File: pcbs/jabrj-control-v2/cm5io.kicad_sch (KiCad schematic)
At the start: 22 parts, among them J801 48406-0003, J802 ARJM11D7-502-AB-EW2, J803 TYPE-C-31-M-12, U801 PESD4USB3BTTS-QX, U802 PESD4USB3BTTS-QX, U803 PESD4USB3BTTS-QX, U804 PESD4USB3BTTS-QX, U805 PESD4USB3BTTS-QX, U806 AP22653FDZ-7, U807 PESD4USB3BTTS-QX

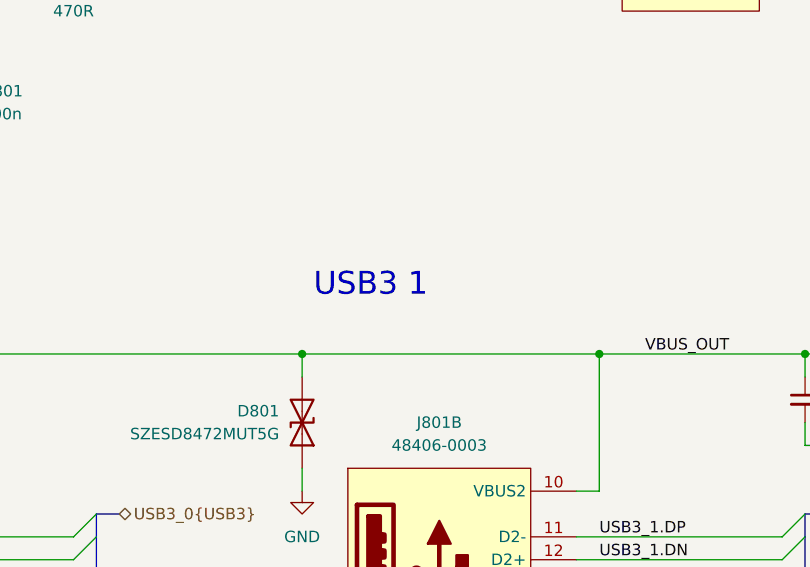
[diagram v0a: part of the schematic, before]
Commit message: Fixed 5V buck inductor value
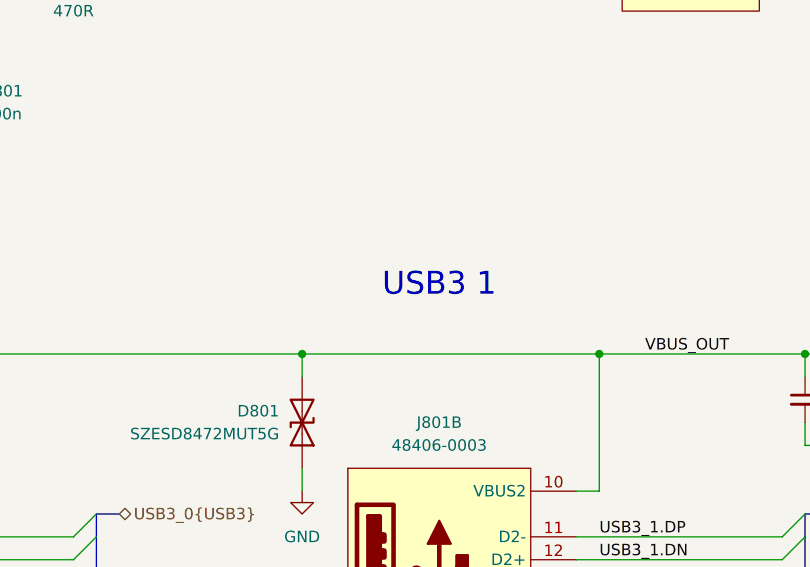
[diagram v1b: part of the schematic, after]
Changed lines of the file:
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@@
 	(text "USB3 1"
 		(exclude_from_sim no)
-		(at 111.76 111.76 0)
+		(at 119.38 111.76 0)
 		(effects
 			(font
@@
 		)
 		(instances
-			(project "jabr-control-v2"
+			(project "jabrj-control-v2"
 				(path "/f91ec272-d09a-4038-bbbb-962739a92c51/adc0b005-3094-4656-96e7-4ee9fb2ab719"
 					(reference "C804")
@@
 		)
 		(instances
-			(project "jabr-control-v2"
+			(project "jabrj-control-v2"
 				(path "/f91ec272-d09a-4038-bbbb-962739a92c51/adc0b005-3094-4656-96e7-4ee9fb2ab719"
 					(reference "#PWR0801")
@@
 		)
 		(instances
-			(project "jabr-control-v2"
+			(project "jabrj-control-v2"
 				(path "/f91ec272-d09a-4038-bbbb-962739a92c51/adc0b005-3094-4656-96e7-4ee9fb2ab719"
 					(reference "J803")
@@
 		)
 		(instances
-			(project "jabr-control-v2"
+			(project "jabrj-control-v2"
 				(path "/f91ec272-d09a-4038-bbbb-962739a92c51/adc0b005-3094-4656-96e7-4ee9fb2ab719"
 					(reference "#PWR0810")
@@
 		)
 		(instances
-			(project "jabr-control-v2"
+			(project "jabrj-control-v2"
 				(path "/f91ec272-d09a-4038-bbbb-962739a92c51/adc0b005-3094-4656-96e7-4ee9fb2ab719"
 					(reference "#PWR0809")
@@
 		)
 		(instances
-			(project "jabr-control-v2"
+			(project "jabrj-control-v2"
 				(path "/f91ec272-d09a-4038-bbbb-962739a92c51/adc0b005-3094-4656-96e7-4ee9fb2ab719"
 					(reference "C807")
@@
 		)
 		(instances
-			(project "jabr-control-v2"
+			(project "jabrj-control-v2"
 				(path "/f91ec272-d09a-4038-bbbb-962739a92c51/adc0b005-3094-4656-96e7-4ee9fb2ab719"
 					(reference "#PWR0817")
@@
 		)
 		(instances
-			(project "jabr-control-v2"
+			(project "jabrj-control-v2"
 				(path "/f91ec272-d09a-4038-bbbb-962739a92c51/adc0b005-3094-4656-96e7-4ee9fb2ab719"
 					(reference "C806")
@@
 		)
 		(instances
-			(project "jabr-control-v2"
+			(project "jabrj-control-v2"
 				(path "/f91ec272-d09a-4038-bbbb-962739a92c51/adc0b005-3094-4656-96e7-4ee9fb2ab719"
 					(reference "U801")
@@
 		)
 		(instances
-			(project "jabr-control-v2"
+			(project "jabrj-control-v2"
 				(path "/f91ec272-d09a-4038-bbbb-962739a92c51/adc0b005-3094-4656-96e7-4ee9fb2ab719"
 					(reference "C801")
@@
 		)
 		(instances
-			(project "jabr-control-v2"
+			(project "jabrj-control-v2"
 				(path "/f91ec272-d09a-4038-bbbb-962739a92c51/adc0b005-3094-4656-96e7-4ee9fb2ab719"
 					(reference "U802")
@@
 		)
 		(instances
-			(project "jabr-control-v2"
+			(project "jabrj-control-v2"
 				(path "/f91ec272-d09a-4038-bbbb-962739a92c51/adc0b005-3094-4656-96e7-4ee9fb2ab719"
 					(reference "#PWR0815")
@@
 		)
 		(instances
-			(project "jabr-control-v2"
+			(project "jabrj-control-v2"
 				(path "/f91ec272-d09a-4038-bbbb-962739a92c51/adc0b005-3094-4656-96e7-4ee9fb2ab719"
 					(reference "D801")
@@
 		)
 		(instances
-			(project "jabr-control-v2"
+			(project "jabrj-control-v2"
 				(path "/f91ec272-d09a-4038-bbbb-962739a92c51/adc0b005-3094-4656-96e7-4ee9fb2ab719"
 					(reference "C805")
@@
 		)
 		(instances
-			(project "jabr-control-v2"
+			(project "jabrj-control-v2"
 				(path "/f91ec272-d09a-4038-bbbb-962739a92c51/adc0b005-3094-4656-96e7-4ee9fb2ab719"
 					(reference "#PWR0808")
@@
 		)
 		(instances
-			(project "jabr-control-v2"
+			(project "jabrj-control-v2"
 				(path "/f91ec272-d09a-4038-bbbb-962739a92c51/adc0b005-3094-4656-96e7-4ee9fb2ab719"
 					(reference "#PWR0812")
@@
 		)
 		(instances
-			(project "jabr-control-v2"
+			(project "jabrj-control-v2"
 				(path "/f91ec272-d09a-4038-bbbb-962739a92c51/adc0b005-3094-4656-96e7-4ee9fb2ab719"
 					(reference "C803")
@@
 		)
 		(instances
-			(project "jabr-control-v2"
+			(project "jabrj-control-v2"
 				(path "/f91ec272-d09a-4038-bbbb-962739a92c51/adc0b005-3094-4656-96e7-4ee9fb2ab719"
 					(reference "#PWR0807")
@@
 		)
 		(instances
-			(project "jabr-control-v2"
+			(project "jabrj-control-v2"
 				(path "/f91ec272-d09a-4038-bbbb-962739a92c51/adc0b005-3094-4656-96e7-4ee9fb2ab719"
 					(reference "#PWR0802")
@@
 		)
 		(instances
-			(project "jabr-control-v2"
+			(project "jabrj-control-v2"
 				(path "/f91ec272-d09a-4038-bbbb-962739a92c51/adc0b005-3094-4656-96e7-4ee9fb2ab719"
 					(reference "U806")
@@
 		)
 		(instances
-			(project "jabr-control-v2"
+			(project "jabrj-control-v2"
 				(path "/f91ec272-d09a-4038-bbbb-962739a92c51/adc0b005-3094-4656-96e7-4ee9fb2ab719"
 					(reference "D802")
@@
 		)
 		(instances
-			(project "jabr-control-v2"
+			(project "jabrj-control-v2"
 				(path "/f91ec272-d09a-4038-bbbb-962739a92c51/adc0b005-3094-4656-96e7-4ee9fb2ab719"
 					(reference "C802")
@@
 		)
 		(instances
-			(project "jabr-control-v2"
+			(project "jabrj-control-v2"
 				(path "/f91ec272-d09a-4038-bbbb-962739a92c51/adc0b005-3094-4656-96e7-4ee9fb2ab719"
 					(reference "#PWR0806")
@@
 		)
 		(instances
-			(project "jabr-control-v2"
+			(project "jabrj-control-v2"
 				(path "/f91ec272-d09a-4038-bbbb-962739a92c51/adc0b005-3094-4656-96e7-4ee9fb2ab719"
 					(reference "#PWR0805")
@@
 		)
 		(instances
-			(project "jabr-control-v2"
+			(project "jabrj-control-v2"
 				(path "/f91ec272-d09a-4038-bbbb-962739a92c51/adc0b005-3094-4656-96e7-4ee9fb2ab719"
 					(reference "U805")
@@
 		)
 		(instances
-			(project "jabr-control-v2"
+			(project "jabrj-control-v2"
 				(path "/f91ec272-d09a-4038-bbbb-962739a92c51/adc0b005-3094-4656-96e7-4ee9fb2ab719"
 					(reference "#PWR0804")
@@
 		)
 		(instances
-			(project "jabr-control-v2"
+			(project "jabrj-control-v2"
 				(path "/f91ec272-d09a-4038-bbbb-962739a92c51/adc0b005-3094-4656-96e7-4ee9fb2ab719"
 					(reference "U804")
@@
 		)
 		(instances
-			(project "jabr-control-v2"
+			(project "jabrj-control-v2"
 				(path "/f91ec272-d09a-4038-bbbb-962739a92c51/adc0b005-3094-4656-96e7-4ee9fb2ab719"
 					(reference "#PWR0813")
@@
 		)
 		(instances
-			(project "jabr-control-v2"
+			(project "jabrj-control-v2"
 				(path "/f91ec272-d09a-4038-bbbb-962739a92c51/adc0b005-3094-4656-96e7-4ee9fb2ab719"
 					(reference "#PWR0814")
@@
 		)
 		(instances
-			(project "jabr-control-v2"
+			(project "jabrj-control-v2"
 				(path "/f91ec272-d09a-4038-bbbb-962739a92c51/adc0b005-3094-4656-96e7-4ee9fb2ab719"
 					(reference "J802")
@@
 		)
 		(instances
-			(project "jabr-control-v2"
+			(project "jabrj-control-v2"
 				(path "/f91ec272-d09a-4038-bbbb-962739a92c51/adc0b005-3094-4656-96e7-4ee9fb2ab719"
 					(reference "#PWR0816")
@@
 		)
 		(instances
-			(project "jabr-control-v2"
+			(project "jabrj-control-v2"
 				(path "/f91ec272-d09a-4038-bbbb-962739a92c51/adc0b005-3094-4656-96e7-4ee9fb2ab719"
 					(reference "#PWR0803")
@@
 		)
 		(instances
-			(project "jabr-control-v2"
+			(project "jabrj-control-v2"
 				(path "/f91ec272-d09a-4038-bbbb-962739a92c51/adc0b005-3094-4656-96e7-4ee9fb2ab719"
 					(reference "R803")
@@
 		)
 		(instances
-			(project "jabr-control-v2"
+			(project "jabrj-control-v2"
 				(path "/f91ec272-d09a-4038-bbbb-962739a92c51/adc0b005-3094-4656-96e7-4ee9fb2ab719"
 					(reference "#PWR0818")
@@
 		)
 		(instances
-			(project "jabr-control-v2"
+			(project "jabrj-control-v2"
 				(path "/f91ec272-d09a-4038-bbbb-962739a92c51/adc0b005-3094-4656-96e7-4ee9fb2ab719"
 					(reference "R802")
@@
 		)
 		(instances
-			(project "jabr-control-v2"
+			(project "jabrj-control-v2"
 				(path "/f91ec272-d09a-4038-bbbb-962739a92c51/adc0b005-3094-4656-96e7-4ee9fb2ab719"
 					(reference "U803")
@@
 		)
 		(instances
-			(project "jabr-control-v2"
+			(project "jabrj-control-v2"
 				(path "/f91ec272-d09a-4038-bbbb-962739a92c51/adc0b005-3094-4656-96e7-4ee9fb2ab719"
 					(reference "J801")
@@
 		)
 		(instances
-			(project "jabr-control-v2"
+			(project "jabrj-control-v2"
 				(path "/f91ec272-d09a-4038-bbbb-962739a92c51/adc0b005-3094-4656-96e7-4ee9fb2ab719"
 					(reference "#PWR0811")
@@
 		)
 		(instances
-			(project "jabr-control-v2"
+			(project "jabrj-control-v2"
 				(path "/f91ec272-d09a-4038-bbbb-962739a92c51/adc0b005-3094-4656-96e7-4ee9fb2ab719"
 					(reference "J801")
@@
 		)
 		(instances
-			(project "jabr-control-v2"
+			(project "jabrj-control-v2"
 				(path "/f91ec272-d09a-4038-bbbb-962739a92c51/adc0b005-3094-4656-96e7-4ee9fb2ab719"
 					(reference "U807")
@@
 		)
 		(instances
-			(project "jabr-control-v2"
+			(project "jabrj-control-v2"
 				(path "/f91ec272-d09a-4038-bbbb-962739a92c51/adc0b005-3094-4656-96e7-4ee9fb2ab719"
 					(reference "R801")

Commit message: Layout started
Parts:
- added J804, J805: FH12-20S-0.5SH, project_footprints:Hirose_FH12-20S-0.5SH_1x20-1MP_P0.50mm_Horizontal, symbol CONN-FPC:FH12-20S-0.5SH
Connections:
- net GND: now also J804.11, J804.14, J804.17, J804.2, J804.20, J804.5, J804.8, J804.MP1, J804.MP2, J805.MP1, J805.MP2
- net USB3_0.DN: now also U805.2 (CH2), U805.9 (NC), J804.4; no longer U802.2 (CH2), U802.9 (NC)
- net USB3_0.DP: now also U805.1 (CH1), U805.10 (NC), J804.3; no longer U802.1 (CH1), U802.10 (NC)
- net USB3_0.RX_N: now also J804.7
- net USB3_0.RX_P: now also J804.6
- net USB3_0.TX_N: now also J804.10
- net USB3_0.TX_P: now also J804.9
- net USB3_1.DN: now also J804.13
- net USB3_1.DP: now also J804.12
- net USB3_1.RX_N: now also U802.2 (CH2), U802.9 (NC), J804.16; no longer U805.2 (CH2), U805.9 (NC)
- net USB3_1.RX_P: now also U802.1 (CH1), U802.10 (NC), J804.15; no longer U805.1 (CH1), U805.10 (NC)
- net USB3_1.TX_N: now also J804.19
- net USB3_1.TX_P: now also J804.18
- net VBUS_EN: now also J804.1

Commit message: Layout almost done
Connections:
- net USB.CC1: now also U807.5 (CH4), U807.6 (NC); no longer U807.2 (CH2), U807.9 (NC)
- net USB.DP: now also U807.2 (CH2), U807.9 (NC); no longer U807.5 (CH4), U807.6 (NC)
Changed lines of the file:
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@@
-	)
-	(junction
-		(at 226.06 50.8)
-		(diameter 0)
-		(color 0 0 0 0)
 	)
 	(junction
@@
 	)
 	(junction
-		(at 231.14 60.96)
-		(diameter 0)
-		(color 0 0 0 0)
-	)
-	(junction
 		(at 66.04 86.36)
 		(diameter 0)
@@
 	)
 	(junction
+		(at 226.06 60.96)
+		(diameter 0)
+		(color 0 0 0 0)
+	)
+	(junction
 		(at 223.52 40.64)
 		(diameter 0)
@@
 	(junction
 		(at 63.5 185.42)
+		(diameter 0)
+		(color 0 0 0 0)
+	)
+	(junction
+		(at 231.14 50.8)
 		(diameter 0)
 		(color 0 0 0 0)
@@
 	(wire
 		(pts
-			(xy 231.14 60.96) (xy 231.14 81.28)
-		)
-		(stroke
-			(width 0)
-			(type default)
-		)
-	)
-	(wire
-		(pts
 			(xy 233.68 78.74) (xy 236.22 78.74)
 		)
@@
 	(wire
 		(pts
-			(xy 223.52 50.8) (xy 226.06 50.8)
+			(xy 223.52 50.8) (xy 231.14 50.8)
 		)
 		(stroke
@@
 	(wire
 		(pts
+			(xy 231.14 50.8) (xy 231.14 81.28)
+		)
+		(stroke
+			(width 0)
+			(type default)
+		)
+	)
+	(wire
+		(pts
 			(xy 208.28 129.54) (xy 208.28 132.08)
 		)
@@
 	(wire
 		(pts
+			(xy 226.06 60.96) (xy 226.06 86.36)
+		)
+		(stroke
+			(width 0)
+			(type default)
+		)
+	)
+	(wire
+		(pts
 			(xy 55.88 142.24) (xy 78.74 142.24)
 		)
@@
 	(wire
 		(pts
-			(xy 231.14 60.96) (xy 248.92 60.96)
-		)
-		(stroke
-			(width 0)
-			(type default)
-		)
-	)
-	(wire
-		(pts
 			(xy 162.56 76.2) (xy 160.02 76.2)
 		)
@@
 		)
 	)
-	(wire
-		(pts
-			(xy 226.06 50.8) (xy 248.92 50.8)
-		)
-		(stroke
-			(width 0)
-			(type default)
-		)
-	)
 	(bus
 		(pts
@@
 	(wire
 		(pts
+			(xy 226.06 60.96) (xy 248.92 60.96)
+		)
+		(stroke
+			(width 0)
+			(type default)
+		)
+	)
+	(wire
+		(pts
 			(xy 58.42 119.38) (xy 104.14 119.38)
 		)
@@
 	(wire
 		(pts
-			(xy 220.98 60.96) (xy 231.14 60.96)
+			(xy 220.98 60.96) (xy 226.06 60.96)
 		)
 		(stroke
@@
 	(wire
 		(pts
+			(xy 231.14 50.8) (xy 248.92 50.8)
+		)
+		(stroke
+			(width 0)
+			(type default)
+		)
+	)
+	(wire
+		(pts
 			(xy 220.98 43.18) (xy 223.52 43.18)
 		)
 		(stroke
-			(width 0)
-			(type default)
-		)
-	)
-	(wire
-		(pts
-			(xy 226.06 50.8) (xy 226.06 86.36)
-		)
-		(stroke

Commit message: 603 Unrouted
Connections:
- net USB3_0.DN: now also J801.2 (D1-), J804.6, U801.4 (CH3), U801.7 (NC); no longer J801.3 (D1+), J804.4, U805.2 (CH2), U805.9 (NC)
- net USB3_0.DP: now also J801.3 (D1+), J804.7, U801.5 (CH4), U801.6 (NC); no longer J801.2 (D1-), J804.3, U805.1 (CH1), U805.10 (NC)
- net USB3_0.RX_N: now also J801.5 (SSRX1-), J804.10, U805.2 (CH2), U805.9 (NC); no longer J801.6 (SSRX1+), J804.7, U801.2 (CH2), U801.9 (NC)
- net USB3_0.RX_P: now also J801.6 (SSRX1+), J804.9, U805.1 (CH1), U805.10 (NC); no longer J801.5 (SSRX1-), J804.6, U801.1 (CH1), U801.10 (NC)
- net USB3_0.TX_N: now also J801.8 (SSTX1-), J804.4, U801.2 (CH2), U801.9 (NC); no longer J801.9 (SSTX1+), J804.10, U801.5 (CH4), U801.6 (NC)
- net USB3_0.TX_P: now also J801.9 (SSTX1+), J804.3, U801.1 (CH1), U801.10 (NC); no longer J801.8 (SSTX1-), J804.9, U801.4 (CH3), U801.7 (NC)
- net USB3_1.DN: now also J801.11 (D2-), J804.16, U802.2 (CH2), U802.9 (NC); no longer J801.12 (D2+), J804.13, U802.5 (CH4), U802.6 (NC)
- net USB3_1.DP: now also J801.12 (D2+), J804.15, U802.1 (CH1), U802.10 (NC); no longer J801.11 (D2-), J804.12, U802.4 (CH3), U802.7 (NC)
- net USB3_1.RX_N: now also J801.14 (SSRX2-), J804.12, U805.4 (CH3), U805.7 (NC); no longer J801.15 (SSRX2+), J804.16, U802.2 (CH2), U802.9 (NC)
- net USB3_1.RX_P: now also J801.15 (SSRX2+), J804.13, U805.5 (CH4), U805.6 (NC); no longer J801.14 (SSRX2-), J804.15, U802.1 (CH1), U802.10 (NC)
- net USB3_1.TX_N: now also J801.17 (SSTX2-), J804.18, U802.4 (CH3), U802.7 (NC); no longer J801.18 (SSTX2+), J804.19, U805.5 (CH4), U805.6 (NC)
- net USB3_1.TX_P: now also J801.18 (SSTX2+), J804.19, U802.5 (CH4), U802.6 (NC); no longer J801.17 (SSTX2-), J804.18, U805.4 (CH3), U805.7 (NC)
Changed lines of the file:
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@@
 		)
 	)
+	(text_box "Superspeed pairs are allowed to swap + and - to ease routing"
+		(exclude_from_sim no)
+		(at -48.26 192.6224 0)
+		(size 25.4 8.0376)
+		(margins 0.9525 0.9525 0.9525 0.9525)
+		(stroke
+			(width 0)
+			(type solid)
+		)
+		(fill
+			(type none)
+		)
+		(effects
+			(font
+				(size 1.27 1.27)
+			)
+			(justify left)
+		)
+	)
 	(text_box "I_{LIM} = 2185mA"
 		(exclude_from_sim no)
@@
 	)
 	(label "USB3_1.DN"
-		(at -17.78 149.86 180)
+		(at -17.78 157.48 180)
 		(effects
 			(font
@@
 	)
 	(label "USB3_0.DP"
-		(at -17.78 124.46 180)
+		(at -17.78 134.62 180)
 		(effects
 			(font
@@
 	)
 	(label "USB3_1.RX_N"
-		(at 137.16 149.86 0)
+		(at 137.16 147.32 0)
 		(effects
 			(font
@@
 	)
 	(label "USB3_0.TX_N"
-		(at 20.32 185.42 0)
+		(at 20.32 180.34 0)
 		(effects
 			(font
@@
 	)
 	(label "USB3_0.DN"
-		(at 58.42 142.24 0)
+		(at 58.42 139.7 0)
 		(effects
 			(font
@@
 	)
 	(label "USB3_1.DP"
-		(at 71.12 182.88 0)
+		(at 71.12 177.8 0)
 		(effects
 			(font
@@
 	)
 	(label "USB3_1.TX_P"
-		(at -17.78 162.56 180)
+		(at -17.78 165.1 180)
 		(effects
 			(font
@@
 	)
 	(label "USB3_1.TX_N"
-		(at 137.16 157.48 0)
+		(at 137.16 154.94 0)
 		(effects
 			(font
@@
 	)
 	(label "USB3_0.DP"
-		(at 58.42 139.7 0)
+		(at 58.42 142.24 0)
 		(effects
 			(font
@@
 	)
 	(label "USB3_1.DP"
-		(at 137.16 139.7 0)
+		(at 137.16 142.24 0)
 		(effects
 			(font
@@
 	)
 	(label "USB3_1.TX_P"
-		(at 121.92 182.88 0)
+		(at 71.12 185.42 0)
 		(effects
 			(font
@@
 	)
 	(label "USB3_1.DP"
-		(at -17.78 147.32 180)
+		(at -17.78 154.94 180)
 		(effects
 			(font
@@
 	)
 	(label "USB3_1.DN"
-		(at 71.12 185.42 0)
+		(at 71.12 180.34 0)
 		(effects
 			(font
@@
 	)
 	(label "USB3_0.DP"
-		(at 121.92 177.8 0)
+		(at 20.32 185.42 0)
 		(effects
 			(font
@@
 	)
 	(label "USB3_0.TX_N"
-		(at -17.78 142.24 180)
+		(at -17.78 127 180)
 		(effects
 			(font
@@
 	)
 	(label "USB3_1.TX_P"
-		(at 137.16 154.94 0)
+		(at 137.16 157.48 0)
 		(effects
 			(font
@@
 	)
 	(label "USB3_0.TX_P"
-		(at -17.78 139.7 180)
+		(at -17.78 124.46 180)
 		(effects
 			(font
@@
 	)
 	(label "USB3_0.RX_N"
-		(at -17.78 134.62 180)
+		(at -17.78 142.24 180)
 		(effects
 			(font
@@
 	)
 	(label "USB3_1.RX_P"
-		(at -17.78 154.94 180)
+		(at -17.78 149.86 180)
 		(effects
 			(font
@@
 	)
 	(label "USB3_0.RX_P"
-		(at 20.32 177.8 0)
+		(at 121.92 177.8 0)
 		(effects
 			(font
@@
 	)
 	(label "USB3_0.TX_P"
-		(at 20.32 182.88 0)
+		(at 20.32 177.8 0)
 		(effects
 			(font
@@
 	)
 	(label "USB3_1.RX_N"
-		(at -17.78 157.48 180)
+		(at -17.78 147.32 180)
 		(effects
 			(font
@@
 	)
 	(label "USB3_1.DN"
-		(at 137.16 142.24 0)
+		(at 137.16 139.7 0)
 		(effects
 			(font
@@
 	)
 	(label "USB3_1.RX_P"
-		(at 137.16 147.32 0)
+		(at 137.16 149.86 0)
 		(effects
 			(font
@@
 	)
 	(label "USB3_0.RX_N"
-		(at 20.32 180.34 0)
+		(at 121.92 180.34 0)
 		(effects
 			(font
@@
 	)
 	(label "USB3_1.RX_P"
-		(at 71.12 177.8 0)
+		(at 121.92 185.42 0)
 		(effects
 			(font
@@
 	)
 	(label "USB3_0.RX_P"
-		(at -17.78 132.08 180)
+		(at -17.78 139.7 180)
 		(effects
 			(font
@@
 	)
 	(label "USB3_0.DN"
-		(at 121.92 180.34 0)
+		(at 20.32 182.88 0)
 		(effects
 			(font
@@
 	)
 	(label "USB3_0.RX_P"
-		(at 58.42 147.32 0)
+		(at 58.42 149.86 0)
 		(effects
 			(font
@@
 	)
 	(label "USB3_0.TX_P"
-		(at 58.42 154.94 0)
+		(at 58.42 157.48 0)
 		(effects
 			(font
@@
 	)
 	(label "USB3_1.TX_N"
-		(at -17.78 165.1 180)
+		(at -17.78 162.56 180)
 		(effects
 			(font
@@
 	)
 	(label "USB3_1.TX_N"
-		(at 121.92 185.42 0)
+		(at 71.12 182.88 0)
 		(effects
 			(font
@@
 	)
 	(label "USB3_0.TX_N"
-		(at 58.42 157.48 0)
+		(at 58.42 154.94 0)
 		(effects
 			(font
@@
 	)
 	(label "USB3_1.RX_N"
-		(at 71.12 180.34 0)
+		(at 121.92 182.88 0)
 		(effects
 			(font
@@
 	)
 	(label "USB3_0.DN"
-		(at -17.78 127 180)
+		(at -17.78 132.08 180)
 		(effects
 			(font
@@
 	)
 	(label "USB3_0.RX_N"
-		(at 58.42 149.86 0)
+		(at 58.42 147.32 0)
 		(effects
 			(font

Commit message: 400 Unrouted
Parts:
- added D803: SZESD8472MUT5G, project_footprints:SZESD7462N2T5G, symbol TVS:SZESD8472MUT5G
- added J806: FFC3A20-05-G, project_footprints:FFC3A2005G, symbol CONN-FPC:FFC3A20-05-G
- added U808: PESD4USB3BTTS-QX, project_footprints:PESD4USB3BTTSQX, symbol TVS:PESD4USB3BTTS-QX
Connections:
- net +3V3: now also J805.20, D803.2 (A2), J806.1
- net ETH.TD_A_N: now also J805.3, U804.2 (CH2), U804.9 (NC); no longer U803.2 (CH2), U803.9 (NC)
- net ETH.TD_A_P: now also J805.2, U804.1 (CH1), U804.10 (NC); no longer U803.1 (CH1), U803.10 (NC)
- net ETH.TD_B_N: now also J805.6, U804.5 (CH4), U804.6 (NC); no longer U803.5 (CH4), U803.6 (NC)
- net ETH.TD_B_P: now also J805.5, U804.4 (CH3), U804.7 (NC); no longer U803.4 (CH3), U803.7 (NC)
- net ETH.TD_C_N: now also J805.9, U803.2 (CH2), U803.9 (NC); no longer U804.2 (CH2), U804.9 (NC)
- net ETH.TD_C_P: now also J805.8, U803.1 (CH1), U803.10 (NC); no longer U804.1 (CH1), U804.10 (NC)
- net ETH.TD_D_N: now also J805.12, U803.5 (CH4), U803.6 (NC); no longer U804.5 (CH4), U804.6 (NC)
- net ETH.TD_D_P: now also J805.11, U803.4 (CH3), U803.7 (NC); no longer U804.4 (CH3), U804.7 (NC)
- net ETH_LED2: now also J805.14
- net ETH_LED3: now also J805.15
- net GND: now also J805.1, J805.10, J805.13, J805.19, J805.4, J805.7, D803.1 (A1), J806.5, U808.3 (GND_1), U808.8 (GND_2)
- net USB.DN: now also U807.2 (CH2), U807.9 (NC); no longer U807.4 (CH3), U807.7 (NC)
- net USB.DP: now also U807.4 (CH3), U807.7 (NC); no longer U807.2 (CH2), U807.9 (NC)
- net RX: now reaches J805.16
- net RX: now also J806.4, U808.1 (CH1), U808.10 (NC)
- net TX: now reaches J805.17
- net TX: now also J806.3, U808.2 (CH2), U808.9 (NC)
- net ~{RST}: now reaches J805.18
- net ~{RST}: now also J806.2, U808.4 (CH3), U808.7 (NC)
- new net: U808.5 (CH4), U808.6 (NC)
- no-connect marks 3 -> 4
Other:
- note added: "Backup FPC Connectors"
- note added: "UART"
- moved on the sheet: C801, C802, C803, C804, C805, C806, C807, D801, D802, J801A, J801B, J802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

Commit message: 133 Unrouted
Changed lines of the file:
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@@
 	(text "UART"
 		(exclude_from_sim no)
-		(at 66.04 43.18 0)
+		(at 66.04 45.72 0)
 		(effects
 			(font
@@
 		)
 	)
-	(text_box "Superspeed pairs are allowed to swap + and - to ease routing"
-		(exclude_from_sim no)
-		(at -58.42 220.5624 0)
-		(size 25.4 8.0376)
-		(margins 0.9525 0.9525 0.9525 0.9525)
-		(stroke
-			(width 0)
-			(type solid)
-		)
-		(fill
-			(type none)
-		)
-		(effects
-			(font
-				(size 1.27 1.27)
-			)
-			(justify left)
-		)
-	)
-	(text_box "When the IO is broken off these FPC connectors can be used to get it back"
+	(text_box "When the IO is broken off these FPC connectors can be used as an alternative"
 		(exclude_from_sim no)
 		(at 88.9 137.2378 0)
